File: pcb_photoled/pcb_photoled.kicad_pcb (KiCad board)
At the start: 2 copper layers, 12 x 19 mm, 4 parts, among them P1 CONN_01X03

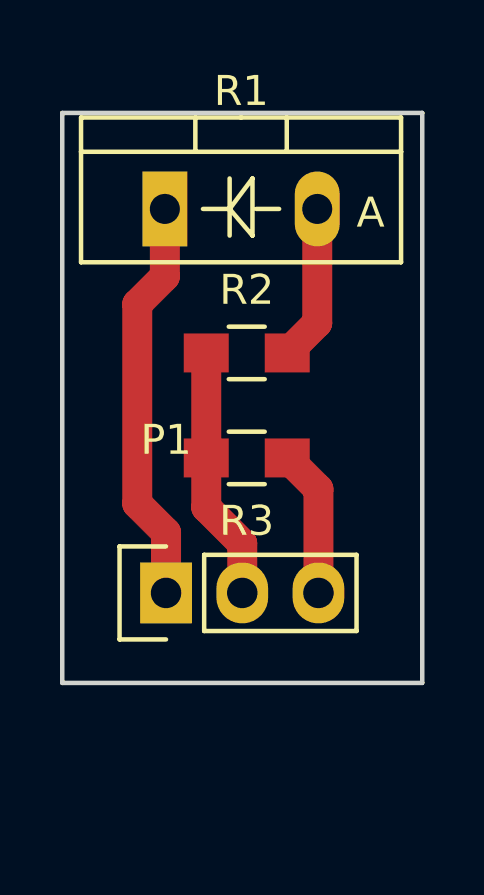
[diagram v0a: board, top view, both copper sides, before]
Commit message: Add a capacitor on the adc line, to suppress noise.
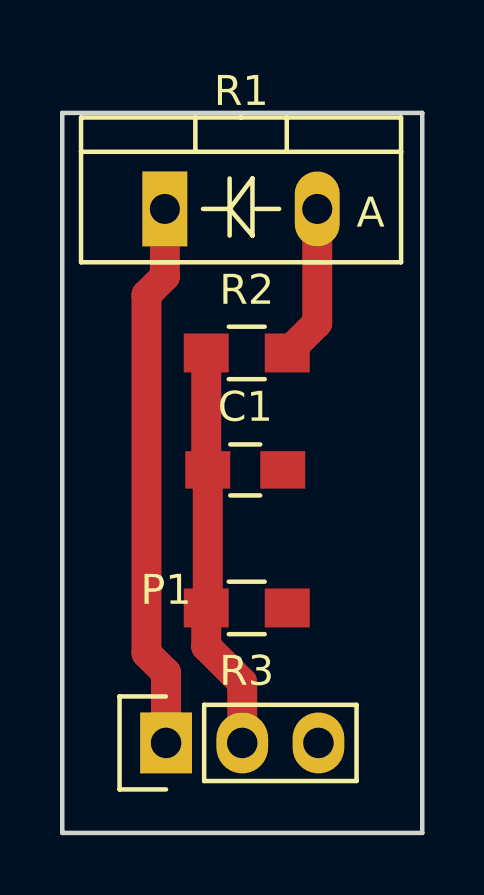
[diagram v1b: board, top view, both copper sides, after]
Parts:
- added C1: 4.7nF, Capacitors_SMD:C_0805_HandSoldering, F.Cu at (145.1, 101.9)
- moved P1 5.00 mm to (142.5, 111.0)
- moved R3 5.00 mm to (145.2, 106.5)
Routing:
- net Net-(C1-Pad1): track 8.50 -> 13.5 mm
- net GND: track 4.93 -> 0.00 mm
- net VCC: track 13.6 -> 18.3 mm
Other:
- board size 12 x 19 mm -> 12 x 24 mm
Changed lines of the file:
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@@
 (kicad_pcb (version 4) (host pcbnew "(2015-12-18 BZR 6383, Git 02d9bbb)-product")
   (general
-    (links 5)
+    (links 7)
     (no_connects 0)
-    (area 138.924999 89.924999 151.075001 109.075001)
+    (area 138.924999 89.924999 151.075001 114.075001)
     (thickness 1.6)
     (drawings 4)
-    (tracks 13)
+    (tracks 14)
     (zones 0)
-    (modules 4)
+    (modules 5)
     (nets 5)
   )
@@
   (net 0 "")
   (net 1 VCC)
-  (net 2 "Net-(P1-Pad2)")
-  (net 3 GND)
-  (net 4 "Net-(R1-Pad2)")
+  (net 2 GND)
+  (net 3 "Net-(R1-Pad2)")
+  (net 4 "Net-(C1-Pad1)")
   (net_class Default "This is the default net class."
     (clearance 0.5)
@@
     (uvia_drill 0.1)
     (add_net GND)
-    (add_net "Net-(P1-Pad2)")
+    (add_net "Net-(C1-Pad1)")
     (add_net "Net-(R1-Pad2)")
     (add_net VCC)
   )
   (module Socket_Strips:Socket_Strip_Straight_1x03 (layer F.Cu)
-    (at 142.46 106)
+    (at 142.46 111)
     (descr "Through hole socket strip")
     (tags "socket strip")
@@
       (net 1 VCC))
     (pad 2 thru_hole oval (at 2.54 0) (size 1.7272 2.032) (drill 1.016) (layers *.Cu *.Mask F.SilkS)
-      (net 2 "Net-(P1-Pad2)"))
+      (net 4 "Net-(C1-Pad1)"))
     (pad 3 thru_hole oval (at 5.08 0) (size 1.7272 2.032) (drill 1.016) (layers *.Cu *.Mask F.SilkS)
-      (net 3 GND))
+      (net 2 GND))
     (model Socket_Strips.3dshapes/Socket_Strip_Straight_1x03.wrl
       (at (xyz 0.1 0 0))
@@
       (net 1 VCC))
     (pad 2 thru_hole oval (at 5.08 0 90) (size 2.49936 1.50114) (drill 1.00076) (layers *.Cu *.Mask F.SilkS)
-      (net 4 "Net-(R1-Pad2)"))
+      (net 3 "Net-(R1-Pad2)"))
     (model Diodes_ThroughHole.3dshapes/Diode_TO-220_Vertical.wrl
       (at (xyz 0.1 0 0))
@@
     (fp_line (start -0.6 -0.875) (end 0.6 -0.875) (layer F.SilkS) (width 0.15))
     (pad 1 smd rect (at -1.35 0) (size 1.5 1.3) (layers F.Cu F.Paste F.Mask)
-      (net 2 "Net-(P1-Pad2)"))
+      (net 4 "Net-(C1-Pad1)"))
     (pad 2 smd rect (at 1.35 0) (size 1.5 1.3) (layers F.Cu F.Paste F.Mask)
-      (net 4 "Net-(R1-Pad2)"))
+      (net 3 "Net-(R1-Pad2)"))
     (model Resistors_SMD.3dshapes/R_0805_HandSoldering.wrl
       (at (xyz 0 0 0))
@@
   )
   (module Resistors_SMD:R_0805_HandSoldering (layer F.Cu)
-    (at 145.15 101.5 180)
+    (at 145.15 106.5 180)
     (descr "Resistor SMD 0805, hand soldering")
     (tags "resistor 0805")
@@
     (fp_line (start -0.6 -0.875) (end 0.6 -0.875) (layer F.SilkS) (width 0.15))
     (pad 1 smd rect (at -1.35 0 180) (size 1.5 1.3) (layers F.Cu F.Paste F.Mask)
-      (net 3 GND))
+      (net 2 GND))
     (pad 2 smd rect (at 1.35 0 180) (size 1.5 1.3) (layers F.Cu F.Paste F.Mask)
-      (net 2 "Net-(P1-Pad2)"))
+      (net 4 "Net-(C1-Pad1)"))
     (model Resistors_SMD.3dshapes/R_0805_HandSoldering.wrl
       (at (xyz 0 0 0))
@@
     )
   )
-  (gr_line (start 139 109) (end 139 90) (layer Edge.Cuts) (width 0.15))
-  (gr_line (start 151 109) (end 139 109) (layer Edge.Cuts) (width 0.15))
-  (gr_line (start 151 90) (end 151 109) (layer Edge.Cuts) (width 0.15))
+  (module Capacitors_SMD:C_0805_HandSoldering (layer F.Cu)
+    (at 145.1 101.9)
+    (descr "Capacitor SMD 0805, hand soldering")
+    (tags "capacitor 0805")
+    (attr smd)
+    (fp_text reference C1 (at 0 -2.1) (layer F.SilkS)
+      (effects (font (size 1 1) (thickness 0.15)))
+    )
+    (fp_text value 4.7nF (at 0 2.1) (layer F.Fab)
+      (effects (font (size 1 1) (thickness 0.15)))
+    )
+    (fp_line (start -2.3 -1) (end 2.3 -1) (layer F.CrtYd) (width 0.05))
+    (fp_line (start -2.3 1) (end 2.3 1) (layer F.CrtYd) (width 0.05))
+    (fp_line (start -2.3 -1) (end -2.3 1) (layer F.CrtYd) (width 0.05))
+    (fp_line (start 2.3 -1) (end 2.3 1) (layer F.CrtYd) (width 0.05))
+    (fp_line (start 0.5 -0.85) (end -0.5 -0.85) (layer F.SilkS) (width 0.15))
+    (fp_line (start -0.5 0.85) (end 0.5 0.85) (layer F.SilkS) (width 0.15))
+    (pad 1 smd rect (at -1.25 0) (size 1.5 1.25) (layers F.Cu F.Paste F.Mask)
+      (net 4 "Net-(C1-Pad1)"))
+    (pad 2 smd rect (at 1.25 0) (size 1.5 1.25) (layers F.Cu F.Paste F.Mask)
+      (net 2 GND))
+    (model Capacitors_SMD.3dshapes/C_0805_HandSoldering.wrl
+      (at (xyz 0 0 0))
+      (scale (xyz 1 1 1))
+      (rotate (xyz 0 0 0))
+    )
+  )
+  (gr_line (start 139 114) (end 139 90) (layer Edge.Cuts) (width 0.15))
+  (gr_line (start 151 114) (end 139 114) (layer Edge.Cuts) (width 0.15))
+  (gr_line (start 151 90) (end 151 114) (layer Edge.Cuts) (width 0.15))
   (gr_line (start 139 90) (end 151 90) (layer Edge.Cuts) (width 0.15))
-  (segment (start 142.46 103.984) (end 142.46 106) (width 1) (layer F.Cu) (net 1))
-  (segment (start 141.5 103.024) (end 142.46 103.984) (width 1) (layer F.Cu) (net 1))
-  (segment (start 141.5 96.36968) (end 141.5 103.024) (width 1) (layer F.Cu) (net 1))
-  (segment (start 142.42 95.44968) (end 141.5 96.36968) (width 1) (layer F.Cu) (net 1))
   (segment (start 142.42 93.2) (end 142.42 95.44968) (width 1) (layer F.Cu) (net 1))
-  (segment (start 143.8 101.5) (end 143.8 103.15) (width 1) (layer F.Cu) (net 2))
-  (segment (start 143.8 103.15) (end 145 104.35) (width 1) (layer F.Cu) (net 2))
-  (segment (start 145 104.35) (end 145 106) (width 1) (layer F.Cu) (net 2))
-  (segment (start 143.8 98) (end 143.8 101.5) (width 1) (layer F.Cu) (net 2))
-  (segment (start 146.5 101.5) (end 147.54 102.54) (width 1) (layer F.Cu) (net 3))
-  (segment (start 147.54 102.54) (end 147.54 106) (width 1) (layer F.Cu) (net 3))
-  (segment (start 147.5 93.2) (end 147.5 97) (width 1) (layer F.Cu) (net 4))
-  (segment (start 147.5 97) (end 146.5 98) (width 1) (layer F.Cu) (net 4))
-  (zone (net 3) (net_name GND) (layer F.Cu) (hatch edge 0.508)
+  (segment (start 142.42 95.44968) (end 141.808336 96.061344) (width 1) (layer F.Cu) (net 1))
+  (segment (start 141.808336 96.061344) (end 141.808336 108.008336) (width 1) (layer F.Cu) (net 1))
+  (segment (start 141.808336 108.008336) (end 142.46 108.66) (width 1) (layer F.Cu) (net 1))
+  (segment (start 142.46 108.66) (end 142.46 111) (width 1) (layer F.Cu) (net 1))
+  (segment (start 147.5 93.2) (end 147.5 97) (width 1) (layer F.Cu) (net 3))
+  (segment (start 147.5 97) (end 146.5 98) (width 1) (layer F.Cu) (net 3))
+  (segment (start 143.8 106.5) (end 143.8 107.784) (width 1) (layer F.Cu) (net 4))
+  (segment (start 143.8 107.784) (end 145 108.984) (width 1) (layer F.Cu) (net 4))
+  (segment (start 145 108.984) (end 145 111) (width 1) (layer F.Cu) (net 4))
+  (segment (start 143.85 101.9) (end 143.85 106.45) (width 1) (layer F.Cu) (net 4))
+  (segment (start 143.85 106.45) (end 143.8 106.5) (width 1) (layer F.Cu) (net 4))
+  (segment (start 143.8 98) (end 143.8 101.85) (width 1) (layer F.Cu) (net 4))
+  (segment (start 143.8 101.85) (end 143.85 101.9) (width 1) (layer F.Cu) (net 4))
+  (zone (net 2) (net_name GND) (layer F.Cu) (hatch edge 0.508)
     (connect_pads (clearance 0.5))
     (min_thickness 0.25)
@@
     (polygon
       (pts
-        (xy 139 90) (xy 151 90) (xy 151 109) (xy 139 109)
+        (xy 139 90) (xy 151 90) (xy 151 114) (xy 139 114)
       )
     )

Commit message: Use a SMD footprint for the BPW photodiode.
This revision was etched and used as v1 PCB for the knpowermeter.
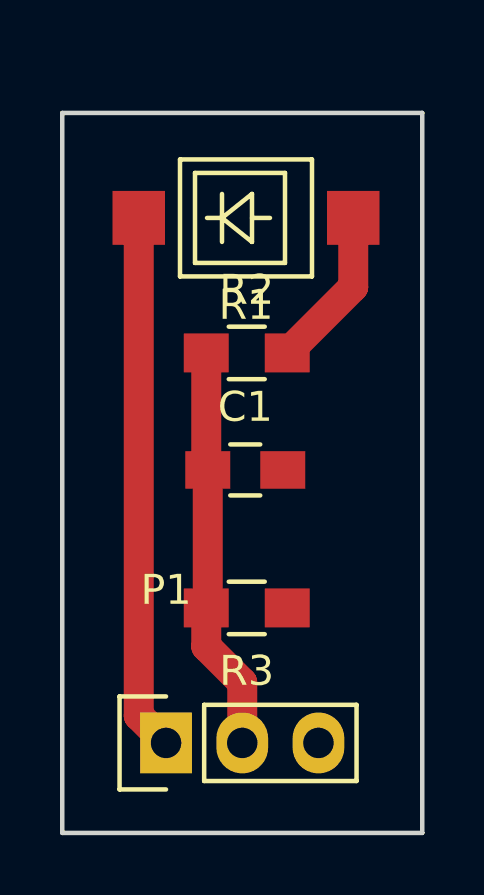
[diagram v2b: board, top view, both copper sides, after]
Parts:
- R1: footprint Diodes_ThroughHole:Diode_TO-220_Vertical -> knielsenlib:VBPW34
- moved R1 2.72 mm to (145.1, 93.5)
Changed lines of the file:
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@@
     (links 7)
     (no_connects 0)
-    (area 138.924999 89.924999 151.075001 114.075001)
+    (area 137.051667 89.275 151.075001 114.075001)
     (thickness 1.6)
     (drawings 4)
-    (tracks 14)
+    (tracks 11)
     (zones 0)
     (modules 5)
@@
     (visible_elements FFFFFF7F)
     (pcbplotparams
-      (layerselection 0x00030_ffffffff)
+      (layerselection 0x00000_7fffffff)
       (usegerberextensions false)
-      (excludeedgelayer true)
+      (excludeedgelayer false)
       (linewidth 0.100000)
       (plotframeref false)
@@
       (outputformat 1)
       (mirror false)
-      (drillshape 1)
+      (drillshape 0)
       (scaleselection 1)
-      (outputdirectory ""))
+      (outputdirectory gerbers/))
   )
   (net 0 "")
@@
     )
   )
-  (module Diodes_ThroughHole:Diode_TO-220_Vertical (layer F.Cu)
-    (at 142.42 93.2)
-    (descr "TO-220, Diode, Vertical,")
-    (tags "TO-220, Diode, Vertical,")
-    (fp_text reference R1 (at 2.54762 -3.92938) (layer F.SilkS)
-      (effects (font (size 1 1) (thickness 0.15)))
-    )
-    (fp_text value Photores (at 2.0701 2.7051) (layer F.Fab)
-      (effects (font (size 1 1) (thickness 0.15)))
-    )
-    (fp_text user A (at 6.858 0.127) (layer F.SilkS)
-      (effects (font (size 1 1) (thickness 0.15)))
-    )
-    (fp_line (start 2.159 0) (end 1.27 0) (layer F.SilkS) (width 0.15))
-    (fp_line (start 3.048 0) (end 3.81 0) (layer F.SilkS) (width 0.15))
-    (fp_line (start 2.159 0) (end 2.921 -1.016) (layer F.SilkS) (width 0.15))
-    (fp_line (start 2.921 -1.016) (end 2.921 0.889) (layer F.SilkS) (width 0.15))
-    (fp_line (start 2.921 0.889) (end 2.159 0) (layer F.SilkS) (width 0.15))
-    (fp_line (start 2.159 -1.016) (end 2.159 0.889) (layer F.SilkS) (width 0.15))
-    (fp_line (start 1.016 -3.048) (end 1.016 -1.905) (layer F.SilkS) (width 0.15))
-    (fp_line (start 4.064 -3.048) (end 4.064 -1.905) (layer F.SilkS) (width 0.15))
-    (fp_line (start 7.874 -1.905) (end 7.874 1.778) (layer F.SilkS) (width 0.15))
-    (fp_line (start 7.874 1.778) (end -2.794 1.778) (layer F.SilkS) (width 0.15))
-    (fp_line (start -2.794 1.778) (end -2.794 -1.905) (layer F.SilkS) (width 0.15))
-    (fp_line (start 7.874 -3.048) (end 7.874 -1.905) (layer F.SilkS) (width 0.15))
-    (fp_line (start 7.874 -1.905) (end -2.794 -1.905) (layer F.SilkS) (width 0.15))
-    (fp_line (start -2.794 -1.905) (end -2.794 -3.048) (layer F.SilkS) (width 0.15))
-    (fp_line (start 2.54 -3.048) (end -2.794 -3.048) (layer F.SilkS) (width 0.15))
-    (fp_line (start 2.54 -3.048) (end 7.874 -3.048) (layer F.SilkS) (width 0.15))
-    (pad 1 thru_hole rect (at 0 0 90) (size 2.49936 1.50114) (drill 1.00076) (layers *.Cu *.Mask F.SilkS)
-      (net 1 VCC))
-    (pad 2 thru_hole oval (at 5.08 0 90) (size 2.49936 1.50114) (drill 1.00076) (layers *.Cu *.Mask F.SilkS)
-      (net 3 "Net-(R1-Pad2)"))
-    (model Diodes_ThroughHole.3dshapes/Diode_TO-220_Vertical.wrl
-      (at (xyz 0.1 0 0))
-      (scale (xyz 0.3937 0.3937 0.3937))
-      (rotate (xyz 0 0 0))
-    )
-  )
   (module Resistors_SMD:R_0805_HandSoldering (layer F.Cu)
     (at 145.15 98)
@@
     )
   )
+  (module knielsenlib:VBPW34 (layer F.Cu)
+    (at 145.125 93.5)
+    (fp_text reference R1 (at 0 2.9) (layer F.SilkS)
+      (effects (font (size 1 1) (thickness 0.15)))
+    )
+    (fp_text value Photores (at 0 -2.8) (layer F.Fab)
+      (effects (font (size 1 1) (thickness 0.15)))
+    )
+    (fp_line (start 0.2 0) (end 0.8 0) (layer F.SilkS) (width 0.15))
+    (fp_line (start -0.8 -0.8) (end -0.8 0.8) (layer F.SilkS) (width 0.15))
+    (fp_line (start -0.8 0) (end -1.3 0) (layer F.SilkS) (width 0.15))
+    (fp_line (start 0.2 0.8) (end -0.8 0) (layer F.SilkS) (width 0.15))
+    (fp_line (start 0.2 -0.8) (end 0.2 0.8) (layer F.SilkS) (width 0.15))
+    (fp_line (start -0.8 0) (end 0.2 -0.8) (layer F.SilkS) (width 0.15))
+    (fp_line (start -1.7 1.5) (end -1.7 -1.5) (layer F.SilkS) (width 0.15))
+    (fp_line (start 1.3 1.5) (end -1.7 1.5) (layer F.SilkS) (width 0.15))
+    (fp_line (start 1.3 -1.5) (end 1.3 1.5) (layer F.SilkS) (width 0.15))
+    (fp_line (start -1.7 -1.5) (end 1.3 -1.5) (layer F.SilkS) (width 0.15))
+    (fp_line (start -2.2 1.95) (end -2.2 -1.95) (layer F.SilkS) (width 0.15))
+    (fp_line (start 2.2 1.95) (end -2.2 1.95) (layer F.SilkS) (width 0.15))
+    (fp_line (start 2.2 -1.95) (end 2.2 1.95) (layer F.SilkS) (width 0.15))
+    (fp_line (start -2.2 -1.95) (end 2.2 -1.95) (layer F.SilkS) (width 0.15))
+    (pad 1 smd rect (at -3.575 0) (size 1.75 1.8) (layers F.Cu F.Paste F.Mask)
+      (net 1 VCC))
+    (pad 2 smd rect (at 3.575 0) (size 1.75 1.8) (layers F.Cu F.Paste F.Mask)
+      (net 3 "Net-(R1-Pad2)"))
+  )
   (gr_line (start 139 114) (end 139 90) (layer Edge.Cuts) (width 0.15))
   (gr_line (start 151 114) (end 139 114) (layer Edge.Cuts) (width 0.15))
   (gr_line (start 151 90) (end 151 114) (layer Edge.Cuts) (width 0.15))
   (gr_line (start 139 90) (end 151 90) (layer Edge.Cuts) (width 0.15))
-  (segment (start 142.42 93.2) (end 142.42 95.44968) (width 1) (layer F.Cu) (net 1))
-  (segment (start 142.42 95.44968) (end 141.808336 96.061344) (width 1) (layer F.Cu) (net 1))
-  (segment (start 141.808336 96.061344) (end 141.808336 108.008336) (width 1) (layer F.Cu) (net 1))
-  (segment (start 141.808336 108.008336) (end 142.46 108.66) (width 1) (layer F.Cu) (net 1))
-  (segment (start 142.46 108.66) (end 142.46 111) (width 1) (layer F.Cu) (net 1))
-  (segment (start 147.5 93.2) (end 147.5 97) (width 1) (layer F.Cu) (net 3))
-  (segment (start 147.5 97) (end 146.5 98) (width 1) (layer F.Cu) (net 3))
+  (segment (start 141.55 93.5) (end 141.55 110.09) (width 1) (layer F.Cu) (net 1))
+  (segment (start 141.55 110.09) (end 142.46 111) (width 1) (layer F.Cu) (net 1))
+  (segment (start 148.7 93.5) (end 148.7 95.8) (width 1) (layer F.Cu) (net 3))
+  (segment (start 148.7 95.8) (end 146.5 98) (width 1) (layer F.Cu) (net 3))
   (segment (start 143.8 106.5) (end 143.8 107.784) (width 1) (layer F.Cu) (net 4))
   (segment (start 143.8 107.784) (end 145 108.984) (width 1) (layer F.Cu) (net 4))
